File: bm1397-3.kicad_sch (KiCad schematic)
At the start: 57 parts, among them IC1 BM1397_mode1, U5 MCP1824T-1802E, U6 MCP1824T-0802E

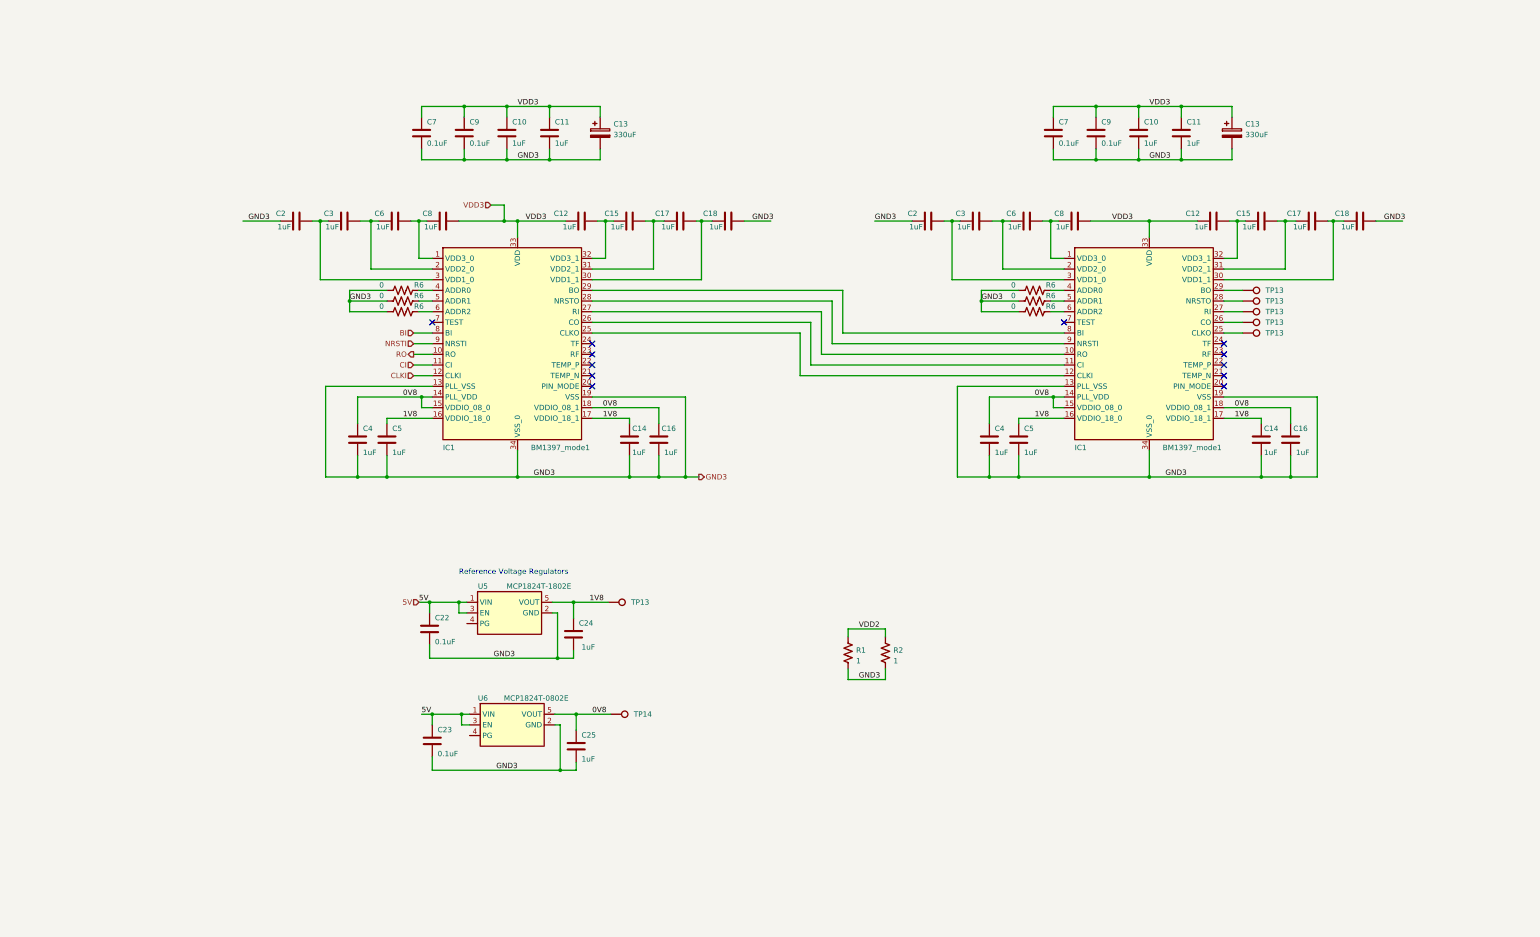
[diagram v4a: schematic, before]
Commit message: some more placements, added level shifters..
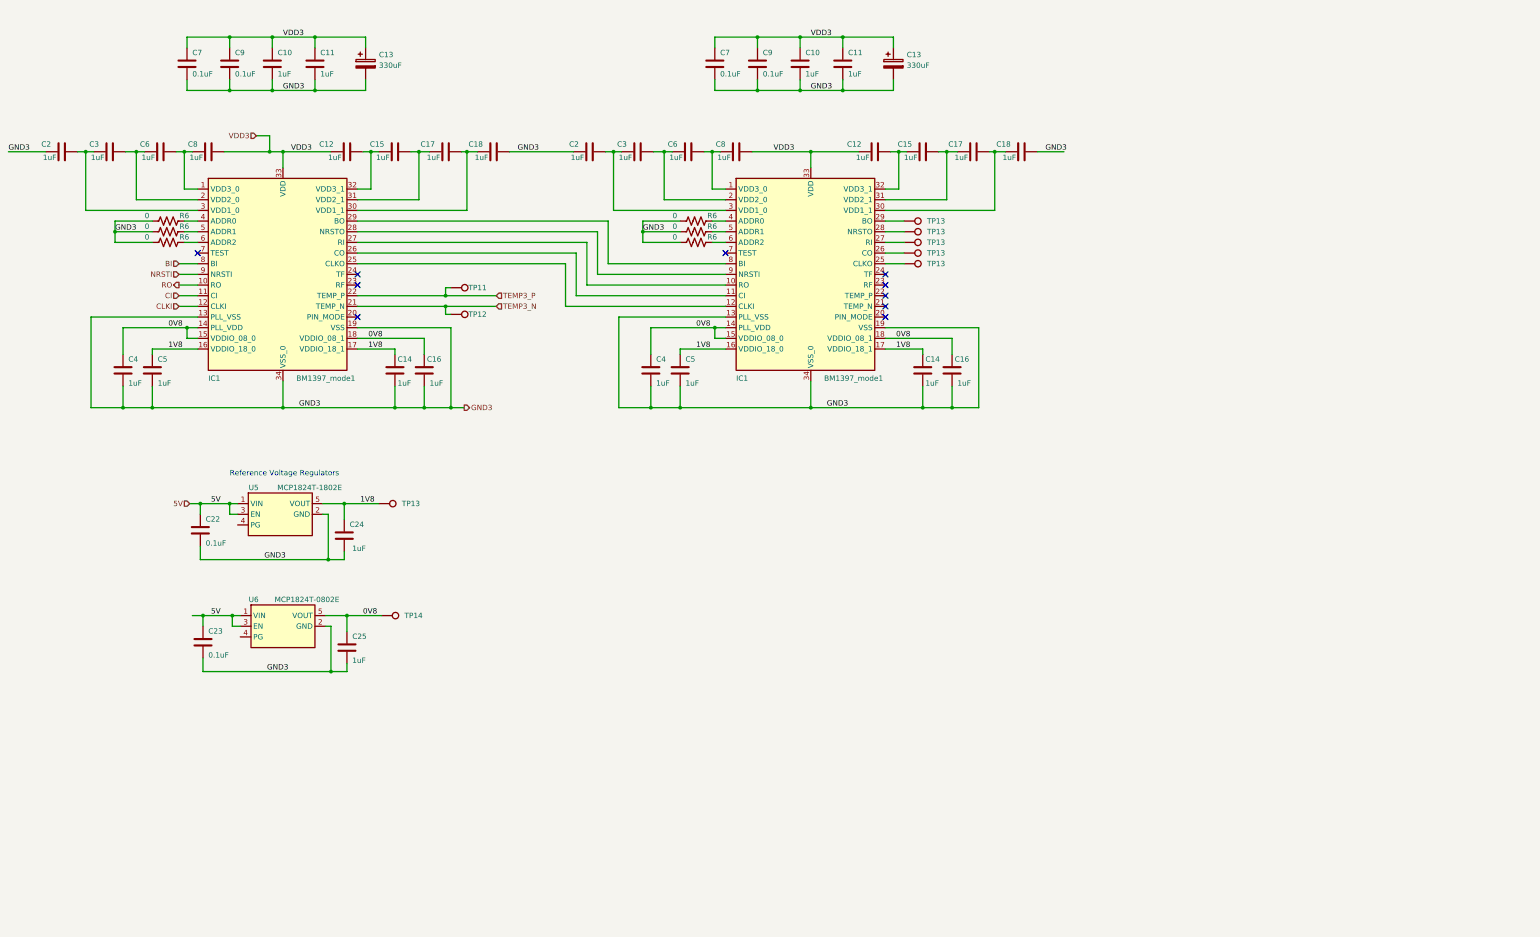
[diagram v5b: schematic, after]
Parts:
- removed R1, R2: 1, Resistor_SMD:R_2512_6332Metric, symbol Device:R_US
- added TP11, TP12: TestPoint, TestPoint:TestPoint_Pad_D1.5mm, symbol Connector:TestPoint
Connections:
- net TEMP3_N: now reaches IC1.21 (TEMP_N)
- net TEMP3_N: now also TP12.1
- net TEMP3_P: now reaches IC1.22 (TEMP_P)
- net TEMP3_P: now also TP11.1
- no-connect marks 12 -> 10
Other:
- moved on the sheet: C10, C11, C12, C13, C14, C15, C16, C17, C18, C2, C22, C23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
